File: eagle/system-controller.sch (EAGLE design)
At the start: 234 parts, among them CN1 22u, IC1 TS4100, J1 1, Q0 MOSFET-P-N-PAIR, Q1 MOSFET-P-N-PAIR, Q10 DNP/NTR4101P, Q11 DNP/NTR4101P, Q12 DNP/NTR4101P, Q13 DON3035L, Q2 MOSFET-P-N-PAIR, Q3 MOSFET-P-N-PAIR, Q4 MOSFET-P-N-PAIR, Q5 MOSFET-P-N-PAIR, Q6 MOSFET-P-N-PAIR, Q7 MOSFET-P-N-PAIR, Q9 DNP/NTR4101P, SW0 TPS25944LRVCRWQFN-20-3X4, SW1 TPS25944LRVCRWQFN-20-3X4, SW2 TPS25944LRVCRWQFN-20-3X4, SW3 TPS25944LRVCRWQFN-20-3X4, SW4 TPS25944LRVCRWQFN-20-3X4, SW5 TPS25944LRVCRWQFN-20-3X4, SW6 TPS25944LRVCRWQFN-20-3X4, SW7 TPS25944LRVCRWQFN-20-3X4, U1 MEGA128-A, X1 8 MHz CRYSTAL-ABRACON-ABM3-SMD

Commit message: latest updates added
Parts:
- RN4: value 10k -> 390
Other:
- note added: "DMN62D0U (Vishay) V(TH) min = 0.5V, V(TH) max = 1.0V"
- note added: "To Do: Change Photoresistor to ACPL-M21L"
- note removed: "To Do: Polarity chech (phoroisolator)"
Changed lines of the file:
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@@
 </part>
 <part name="RNR" library="rcl_custom" deviceset="R-US_" device="0603-B-NOSILK" value="470k"/>
-<part name="RN4" library="rcl_custom" deviceset="R-US_" device="0603-B-NOSILK" value="10k"/>
+<part name="RN4" library="rcl_custom" deviceset="R-US_" device="0603-B-NOSILK" value="390"/>
 <part name="GND53" library="psas_c3_team05" deviceset="GND" device=""/>
 <part name="Q13" library="adafruit" deviceset="MOSFET-N" device="REFLOW" value="DON3035L"/>
@@
 <text x="233.68" y="132.08" size="1.778" layer="97">P-Channel MOSFET</text>
 <text x="265.176" y="309.88" size="1.778" layer="99">To Do:
-Polarity chech (phoroisolator)</text>
+Change Photoresistor to ACPL-M21L </text>
+<text x="60.96" y="332.74" size="1.778" layer="95">DMN62D0U  (Vishay)
+V(TH) min = 0.5V, V(TH) max = 1.0V</text>
 </plain>
 <instances>

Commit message: newest changes
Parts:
- removed IC1: TS4100, TQFN16300x300:TS4100
- added IC2: TS4100, system-controller:TS4100
- D1, D2, D3: device SMD-DIODE-SCHOTTKY-40V-5A_DO-214AB_ SSC53L:SMD-DIODE-SCHOTTKY-40V-5A(DO-214AB)-SSC53L -> system-controller:SMD-DIODE-SCHOTTKY-40V-5A(DO-214AB)-SSC53L; DIST digikey -> (none); DPN SSC53L-E3/57TGICT-ND -> (none); MFN SSC53L-E3/57T -> (none); MPN Vishay -> (none)
- SW0: device WQFN-20-3x4:TPS25944LRVCRWQFN-20-3X4 -> system-controller:TPS25944LRVCRWQFN-20-3X4; DIST digikey -> (none); DPN 296-42152-1-ND -> (none); MFN TPS25944LRVCR -> (none); MPN Texas Instruments -> (none)
- SW1, SW2, SW3, SW4, SW5, SW6, SW7: device WQFN-20-3x4:TPS25944LRVCRWQFN-20-3X4 -> system-controller:TPS25944LRVCRWQFN-20-3X4
- renumbered CPHOTO0A to C31, CPHOTO1B to C32, CPHOTO3A to C33, CPHOTO3B to C34, RPHOTO0A to R47, RPHOTO0B to R49, RPHOTO1A to R48, RPHOTO1B to R50, RPHOTO2A to R51, RPHOTO2B to R54, RPHOTO3A to R52, RPHOTO3B to R53
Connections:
- net 3V: now also IC2.VDD; no longer IC1.VDD
- net GND: now also IC2.GND, IC2.INH; no longer IC1.GND, IC1.INH
- net N$107: now also IC2.COMM; no longer IC1.COMM
- net N$46: now also IC2.ADDC; no longer IC1.ADDC
- net N$47: now also IC2.ADDB; no longer IC1.ADDB
- net N$48: now also IC2.ADDA; no longer IC1.ADDA
- net VCB0_IMON: now also IC2.NO0\; no longer IC1.NO0\
- net VCB1_IMON: now also IC2.NO1; no longer IC1.NO1
- net VCB2_IMON: now also IC2.NO2; no longer IC1.NO2
- net VCB3_IMON: now also IC2.NO3; no longer IC1.NO3
- net VCB4_IMON: now also IC2.NO4; no longer IC1.NO4
- net VCB5_IMON: now also IC2.NO5; no longer IC1.NO5
- net VCB6_IMON: now also IC2.NO6; no longer IC1.NO6
- net VCB7_IMON: now also IC2.NO7; no longer IC1.NO7
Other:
- note added: "Assuming 3V at each pin: When all three pins are high the voltage at TP43 is 2.25V When two pins are high the voltage at TP43 is 1.5V When all three pins are high the voltage at TP43 is 0.75V"
- note added: "Look for TPs connected to GND!!!!!!"
- note removed: "N-Channel MOSFET DON3053L V_TH min = 0.6V V_TH max = 1.4V"
- note removed: "To Do: Change Photoresistor to ACPL-M21L"

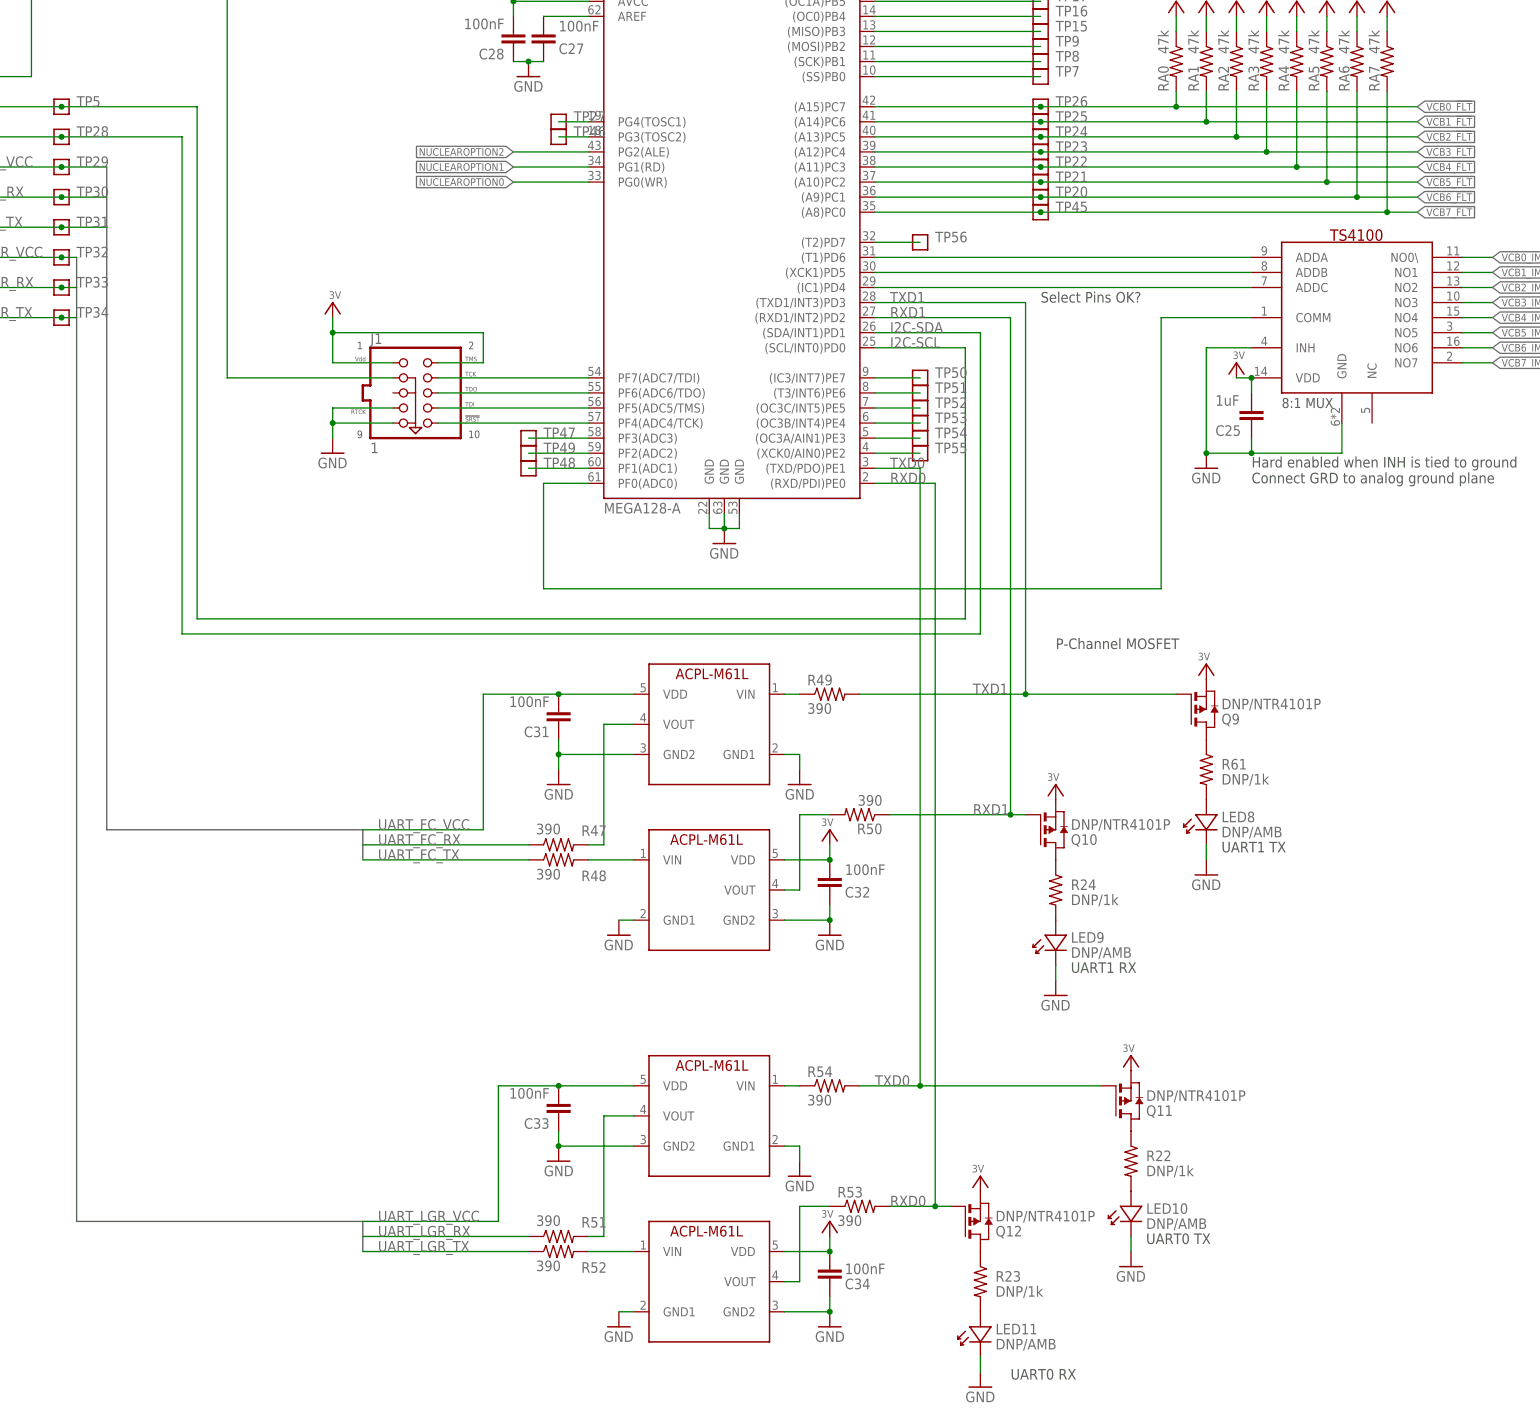
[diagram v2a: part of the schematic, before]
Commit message: final changes pushed for the day: change to optical isolation circuitry and board fixes due to this
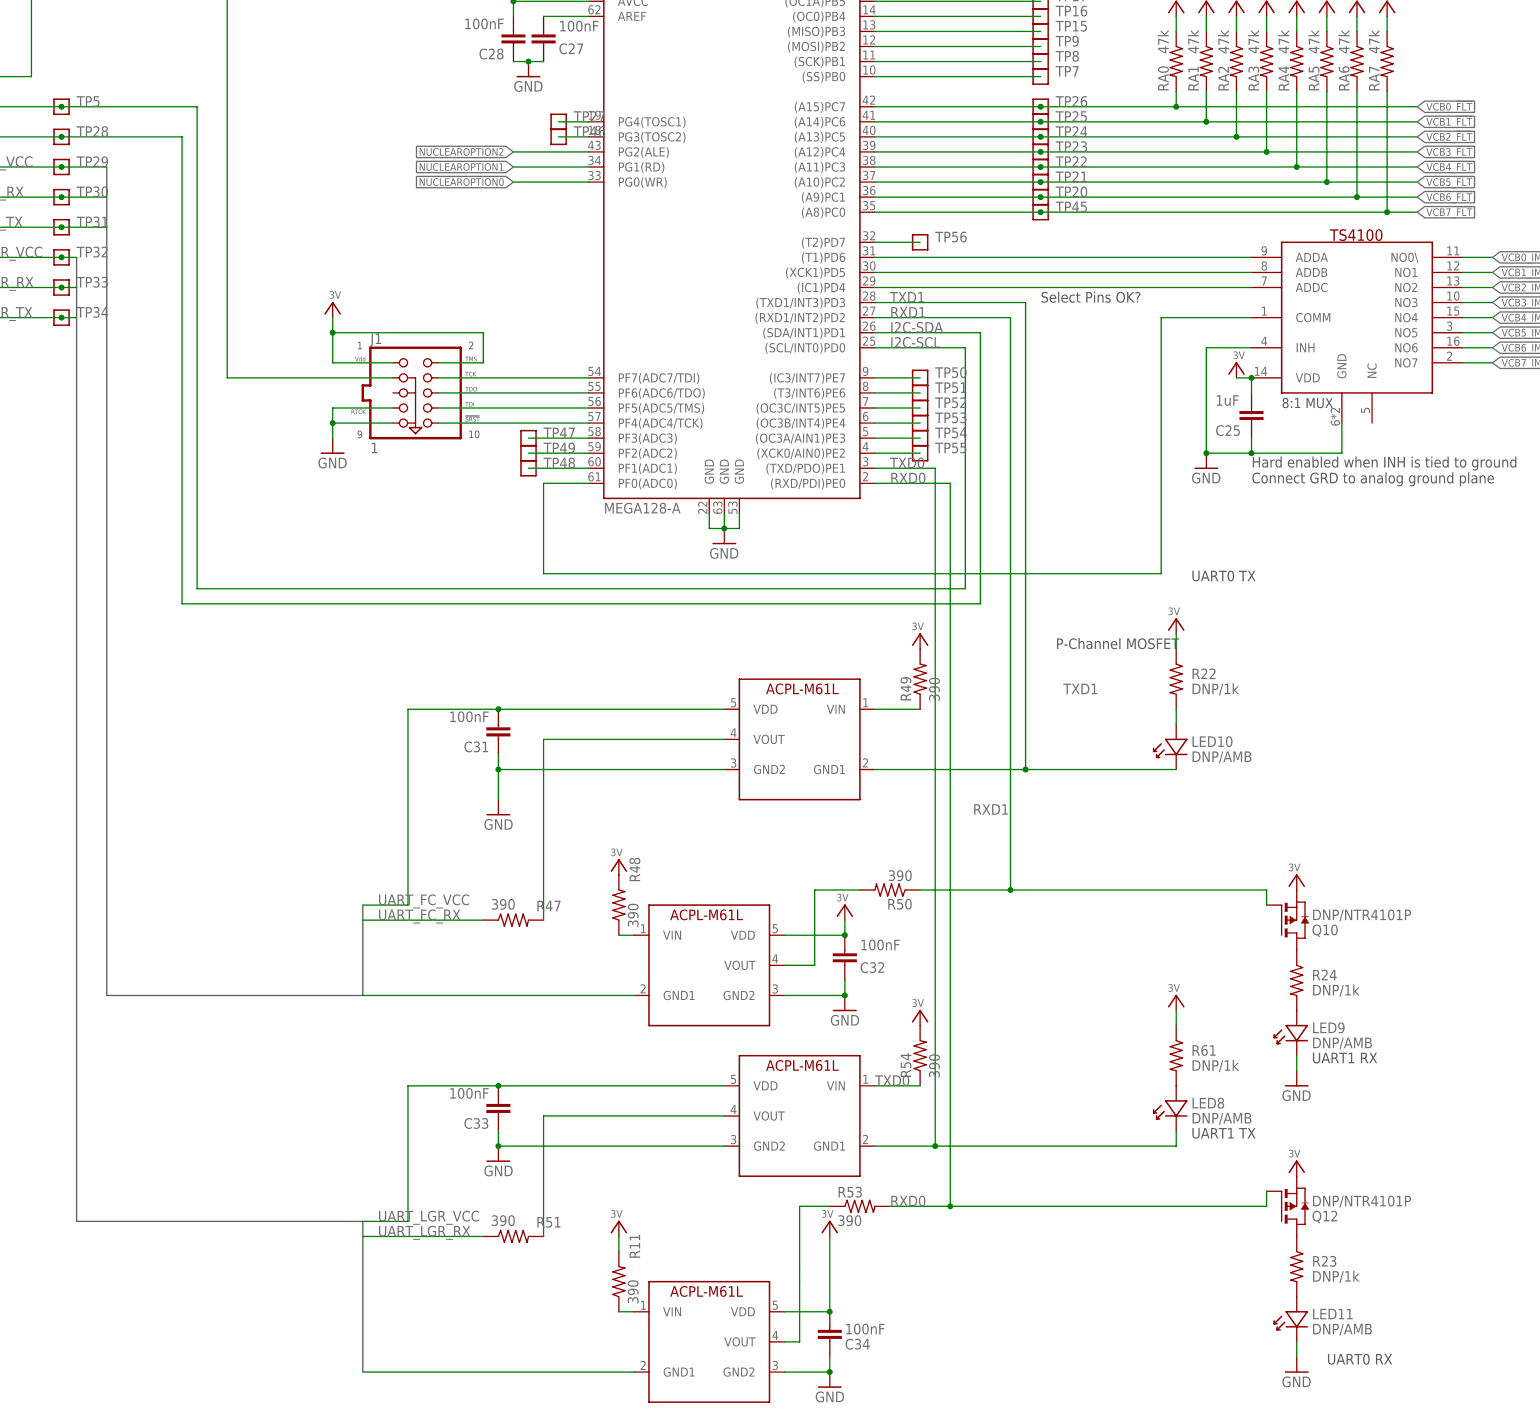
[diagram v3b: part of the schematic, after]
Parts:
- removed Q11, Q9: DNP/NTR4101P, Tova:NTR4101P
- removed R52: 390, rcl_custom:R-US_0603-B-NOSILK
- added R11: 390, rcl_custom:R-US_0603-B-NOSILK
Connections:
- removed net N$20: R52.2, U$4.VIN
- removed net N$58 (its old number): Q9.D, R61.1
- net 3V: now also R11.2, R22.1, R48.2, R49.2, R54.2, R61.1; no longer Q11.S, Q9.S
- net GND: no longer LED10.K, LED8.K, U$1.GND1, U$2.GND1, U$3.GND1, U$4.GND1
- net N$54: now also R11.1, U$4.VIN; no longer Q11.D, R22.1
- net N$8: now also R48.1; no longer R48.2
- net TXD0: now also LED8.K, U$3.GND1; no longer Q11.G, R54.2
- net TXD1: now also LED10.K, U$1.GND1; no longer Q9.G, R49.2
- net UART_FC_TX: now also U$2.GND1; no longer R48.1
- net UART_LGR_TX: now also U$4.GND1; no longer R52.1
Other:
- note removed: "CHECK POLARITY"
- moved on the sheet: C31, C32, C33, C34, LED10, LED11, LED8, LED9, Q10, Q12, R22, R23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
